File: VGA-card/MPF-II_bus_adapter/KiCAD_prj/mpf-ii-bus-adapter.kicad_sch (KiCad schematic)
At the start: 34 parts, among them J1 Bus_Apple_II_Card_Side, J10 USER1_Sel, J11 INH_Sel, J12 RDY_Sel, J13 COLREF_Sel, J14 IOSTRB_Sel, J15 Q3_Sel, J16 Pin, J17 Pin, J18 Pin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

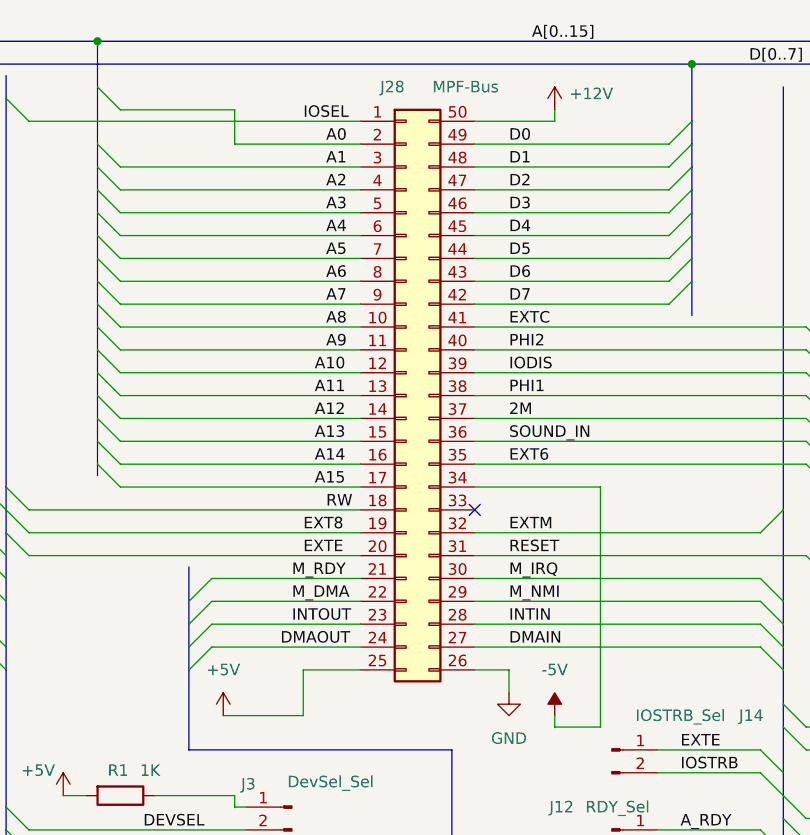
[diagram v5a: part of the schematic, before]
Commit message: PCB connector updated
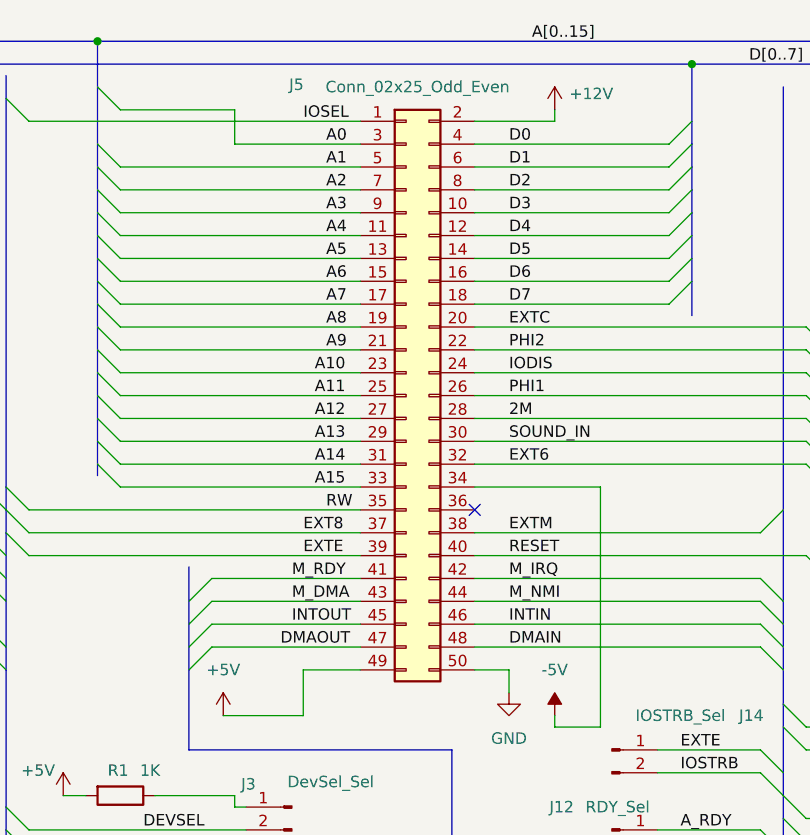
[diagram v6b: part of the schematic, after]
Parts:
- removed J28: MPF-Bus, Connector_PinHeader_2.54mm:PinHeader_2x25_P2.54mm_Vertical, symbol Connector_Generic:Conn_02x25_Counter_Clockwise
- added J5: Conn_02x25_Odd_Even, Connector_PinHeader_2.54mm:PinHeader_2x25_P2.54mm_Vertical, symbol Connector_Generic:Conn_02x25_Odd_Even
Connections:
- net +12V: now also J5.2 (Pin_2)
- net +5V: now also J5.49 (Pin_49)
- net -5V: now also J5.34 (Pin_34)
- net 2M: now also J5.28 (Pin_28)
- net A0: now also J5.3 (Pin_3)
- net A1: now also J5.5 (Pin_5)
- net A10: now also J5.23 (Pin_23)
- net A11: now also J5.25 (Pin_25)
- net A12: now also J5.27 (Pin_27)
- net A13: now also J5.29 (Pin_29)
- net A14: now also J5.31 (Pin_31)
- net A15: now also J5.33 (Pin_33)
- net A2: now also J5.7 (Pin_7)
- net A3: now also J5.9 (Pin_9)
- net A4: now also J5.11 (Pin_11)
- net A5: now also J5.13 (Pin_13)
- net A6: now also J5.15 (Pin_15)
- net A7: now also J5.17 (Pin_17)
- net A8: now also J5.19 (Pin_19)
- net A9: now also J5.21 (Pin_21)
- net D0: now also J5.4 (Pin_4)
- net D1: now also J5.6 (Pin_6)
- net D2: now also J5.8 (Pin_8)
- net D3: now also J5.10 (Pin_10)
- net D4: now also J5.12 (Pin_12)
- net D5: now also J5.14 (Pin_14)
- net D6: now also J5.16 (Pin_16)
- net D7: now also J5.18 (Pin_18)
- net DMAIN: now also J5.48 (Pin_48)
- net DMAOUT: now also J5.47 (Pin_47)
- net EXT6: now also J5.32 (Pin_32)
- net EXT8: now also J5.37 (Pin_37)
- net EXTC: now also J5.20 (Pin_20)
- net EXTE: now also J5.39 (Pin_39)
- net EXTM: now also J5.38 (Pin_38)
- net GND: now also J5.50 (Pin_50)
- net INTIN: now also J5.46 (Pin_46)
- net INTOUT: now also J5.45 (Pin_45)
- net IODIS: now also J5.24 (Pin_24)
- net IOSEL: now also J5.1 (Pin_1)
- net M_DMA: now also J5.43 (Pin_43)
- net M_IRQ: now also J5.42 (Pin_42)
- net M_NMI: now also J5.44 (Pin_44)
- net M_RDY: now also J5.41 (Pin_41)
- net PHI1: now also J5.26 (Pin_26)
- net PHI2: now also J5.22 (Pin_22)
- net RESET: now also J5.40 (Pin_40)
- net RW: now also J5.35 (Pin_35)
- net SOUND_IN: now also J5.30 (Pin_30)
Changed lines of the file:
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@@
 	(title_block
 		(title "Microprofessor-II Bus Adapter Board")
-		(date "2024-07-26")
+		(date "2024-07-29")
 		(rev "A")
 		(comment 1 "Licensed under CERN-OHL-P V2.0 (https://ohwr.org/cern_ohl_p_v2.txt)")
@@
 	)
 	(symbol
+		(lib_id "Connector_Generic:Conn_02x25_Odd_Even")
+		(at 158.75 54.61 0)
+		(unit 1)
+		(exclude_from_sim no)
+		(in_bom yes)
+		(on_board yes)
+		(dnp no)
+		(property "Reference" "J5"
+			(at 146.558 20.066 0)
+			(effects
+				(font
+					(size 1.27 1.27)
+				)
+			)
+		)
+		(property "Value" "Conn_02x25_Odd_Even"
+			(at 160.02 20.32 0)
+			(effects
+				(font
+					(size 1.27 1.27)
+				)
+			)
+		)
+		(property "Footprint" "Connector_PinHeader_2.54mm:PinHeader_2x25_P2.54mm_Vertical"
+			(at 158.75 54.61 0)
+			(effects
+				(font
+					(size 1.27 1.27)
+				)
+				(hide yes)
+			)
+		)
+		(property "Datasheet" "~"
+			(at 158.75 54.61 0)
+			(effects
+				(font
+					(size 1.27 1.27)
+				)
+				(hide yes)
+			)
+		)
+		(property "Description" "Generic connector, double row, 02x25, odd/even pin numbering scheme (row 1 odd numbers, row 2 even numbers), script generated (kicad-library-utils/schlib/autogen/connector/)"
+			(at 158.75 54.61 0)
+			(effects
+				(font
+					(size 1.27 1.27)
+				)
+				(hide yes)
+			)
+		)
+		(pin "13"
+		)
+		(pin "33"
+		)
+		(pin "18"
+		)
+		(pin "20"
+		)
+		(pin "35"
+		)
+		(pin "49"
+		)
+		(pin "25"
+		)
+		(pin "36"
+		)
+		(pin "22"
+		)
+		(pin "10"
+		)
+		(pin "37"
+		)
+		(pin "11"
+		)
+		(pin "26"
+		)
+		(pin "28"
+		)
+		(pin "15"
+		)
+		(pin "14"
+		)
+		(pin "1"
+		)
+		(pin "17"
+		)
+		(pin "32"
+		)
+		(pin "38"
+		)
+		(pin "39"
+		)
+		(pin "12"
+		)
+		(pin "34"
+		)
+		(pin "24"
+		)
+		(pin "2"
+		)
+		(pin "21"
+		)
+		(pin "19"
+		)
+		(pin "23"
+		)
+		(pin "30"
+		)
+		(pin "29"
+		)
+		(pin "31"
+		)
+		(pin "16"
+		)
+		(pin "3"
+		)
+		(pin "27"
+		)
+		(pin "4"
+		)
+		(pin "43"
+		)
+		(pin "45"
+		)
+		(pin "40"
+		)
+		(pin "6"
+		)
+		(pin "50"
+		)
+		(pin "44"
+		)
+		(pin "46"
+		)
+		(pin "41"
+		)
+		(pin "48"
+		)
+		(pin "47"
+		)
+		(pin "5"
+		)
+		(pin "42"
+		)
+		(pin "8"
+		)
+		(pin "7"
+		)
+		(pin "9"
+		)
+		(instances
+			(project ""
+				(path "/cfc9cf74-9f21-4b66-b98c-dffd14f2b307"
+					(reference "J5")
+					(unit 1)
+				)
+			)
+		)
+	)
+	(symbol
 		(lib_id "Connector:Conn_01x02_Pin")
 		(at 181.61 93.98 0)
@@
 					(unit 1)
 				)
-			)
-		)
-	)
-	(symbol
-		(lib_id "Connector_Generic:Conn_02x25_Counter_Clockwise")
-		(at 158.75 54.61 0)
-		(unit 1)
-		(exclude_from_sim no)
-		(in_bom yes)
-		(on_board yes)
-		(dnp no)
-		(property "Reference" "J28"
-			(at 157.226 20.32 0)
-			(effects
-				(font
-					(size 1.27 1.27)
-				)
-			)
-		)
-		(property "Value" "MPF-Bus"
-			(at 165.354 20.32 0)
-			(effects
-				(font
-					(size 1.27 1.27)
-				)
-			)
-		)
-		(property "Footprint" "Connector_PinHeader_2.54mm:PinHeader_2x25_P2.54mm_Vertical"
-			(at 158.75 54.61 0)
-			(effects
-				(font
-					(size 1.27 1.27)
-				)
-				(hide yes)
-			)
-		)
-		(property "Datasheet" "~"
-			(at 158.75 54.61 0)
-			(effects
-				(font
-					(size 1.27 1.27)
-				)
-				(hide yes)
-			)
-		)
-		(property "Description" "Generic connector, double row, 02x25, counter clockwise pin numbering scheme (similar to DIP package numbering), script generated (kicad-library-utils/schlib/autogen/connector/)"
-			(at 158.75 54.61 0)
-			(effects
-				(font
-					(size 1.27 1.27)
-				)
-				(hide yes)
-			)
-		)
-		(pin "35"
-		)
-		(pin "10"
-		)
-		(pin "42"
-		)
-		(pin "32"
-		)
-		(pin "25"
-		)
-		(pin "43"
-		)
-		(pin "44"
-		)
-		(pin "28"
-		)
-		(pin "47"
-		)
-		(pin "41"
-		)
-		(pin "33"
-		)
-		(pin "45"
-		)
-		(pin "4"
-		)
-		(pin "50"
-		)
-		(pin "6"
-		)
-		(pin "7"
-		)
-		(pin "8"
-		)
-		(pin "12"
-		)
-		(pin "9"
-		)
-		(pin "5"
-		)
-		(pin "26"
-		)
-		(pin "3"
-		)
-		(pin "36"
-		)
-		(pin "16"
-		)
-		(pin "38"
-		)
-		(pin "31"
-		)
-		(pin "21"
-		)
-		(pin "39"
-		)
-		(pin "40"
-		)
-		(pin "13"
-		)
-		(pin "19"
-		)
-		(pin "29"
-		)
-		(pin "46"
-		)
-		(pin "27"
-		)
-		(pin "48"
-		)
-		(pin "11"
-		)
-		(pin "17"
-		)
-		(pin "22"
-		)
-		(pin "49"
-		)
-		(pin "37"
-		)
-		(pin "14"
-		)
-		(pin "15"
-		)
-		(pin "18"
-		)
-		(pin "2"
-		)
-		(pin "1"
-		)
-		(pin "23"
-		)
-		(pin "24"
-		)
-		(pin "30"
-		)
-		(pin "20"
-		)
-		(pin "34"
-		)
-		(instances
-			(project ""
-				(path "/cfc9cf74-9f21-4b66-b98c-dffd14f2b307"
-					(reference "J28")
-					(unit 1)
-				)

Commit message: PCB
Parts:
- removed J16, J17, J18, J19, J20, J21, J22, J23, J24, J25: Pin, Connector_PinHeader_2.00mm:PinHeader_1x01_P2.00mm_Vertical, symbol Connector:Conn_01x01_Pin
- added J16: Conn_01x04_Pin, Connector_PinHeader_2.54mm:PinHeader_1x04_P2.54mm_Vertical, symbol Connector:Conn_01x04_Pin
- added J17: Conn_01x06_Pin, Connector_PinHeader_2.54mm:PinHeader_1x06_P2.54mm_Vertical, symbol Connector:Conn_01x06_Pin
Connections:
- net at U1.9: now also J17.5 (Pin_5)
- net at U1.3: now also J16.1 (Pin_1)
- net at U1.11: now also J17.3 (Pin_3)
- net at U1.10: now also J17.4 (Pin_4)
- net at U1.5: now also J16.3 (Pin_3)
- net at U1.6: now also J16.4 (Pin_4)
- net at U1.12: now also J17.2 (Pin_2)
- net at U1.13: now also J17.1 (Pin_1)
- net at U1.8: now also J17.6 (Pin_6)
- net at U1.4: now also J16.2 (Pin_2)
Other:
- moved on the sheet: U1B, U1C, U1D, U1E, U1F

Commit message: PCB updated
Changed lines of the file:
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@@
 	)
 	(bus_entry
-		(at 203.2 52.07)
-		(size 2.54 2.54)
-		(stroke
-			(width 0)
-			(type default)
-		)
-	)
-	(bus_entry
 		(at 124.46 62.23)
 		(size 2.54 2.54)
@@
 	)
 	(bus_entry
+		(at 198.12 50.8)
+		(size 2.54 2.54)
+		(stroke
+			(width 0)
+			(type default)
+		)
+	)
+	(bus_entry
 		(at 124.46 59.69)
 		(size 2.54 2.54)
@@
 	(wire
 		(pts
-			(xy 166.37 52.07) (xy 203.2 52.07)
-		)
-		(stroke
-			(width 0)
-			(type default)
-		)
-	)
-	(wire
-		(pts
 			(xy 215.9 45.72) (xy 227.33 45.72)
 		)
@@
 	(bus
 		(pts
-			(xy 205.74 54.61) (xy 205.74 57.15)
+			(xy 205.74 52.07) (xy 205.74 57.15)
 		)
 		(stroke
@@
 	(wire
 		(pts
+			(xy 190.5 50.8) (xy 198.12 50.8)
+		)
+		(stroke
+			(width 0)
+			(type default)
+		)
+	)
+	(wire
+		(pts
 			(xy 166.37 69.85) (xy 198.12 69.85)
 		)
@@
 	(bus
 		(pts
-			(xy 205.74 52.07) (xy 205.74 54.61)
-		)
-		(stroke
-			(width 0)
-			(type default)
-		)
-	)
-	(bus
-		(pts
 			(xy 200.66 105.41) (xy 200.66 106.68)
 		)
@@
 	(bus
 		(pts
+			(xy 200.66 53.34) (xy 200.66 67.31)
+		)
+		(stroke
+			(width 0)
+			(type default)
+		)
+	)
+	(bus
+		(pts
 			(xy 124.46 15.24) (xy 124.46 20.32)
 		)
@@
 	(wire
 		(pts
+			(xy 166.37 52.07) (xy 190.5 52.07)
+		)
+		(stroke
+			(width 0)
+			(type default)
+		)
+	)
+	(wire
+		(pts
 			(xy 96.52 72.39) (xy 111.76 72.39)
 		)
@@
 	(bus
 		(pts
-			(xy 200.66 20.32) (xy 200.66 67.31)
+			(xy 200.66 20.32) (xy 200.66 53.34)
 		)
 		(stroke
@@
 		)
 		(stroke
+			(width 0)
+			(type default)
+		)
+	)
+	(wire
+		(pts
+			(xy 190.5 52.07) (xy 190.5 50.8)
+		)
+		(stroke
